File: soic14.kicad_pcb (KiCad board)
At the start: 2 copper layers, 11.2 x 27.4 mm, 2 parts, among them J1 Conn_02x07_Counter_Clockwise, J2 Conn_02x07_Counter_Clockwise

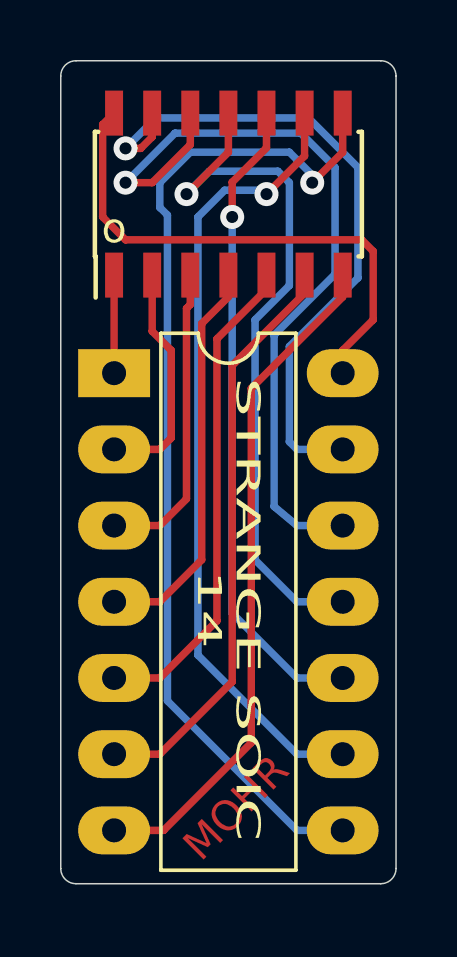
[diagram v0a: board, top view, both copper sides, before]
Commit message: fixed DRC warning.
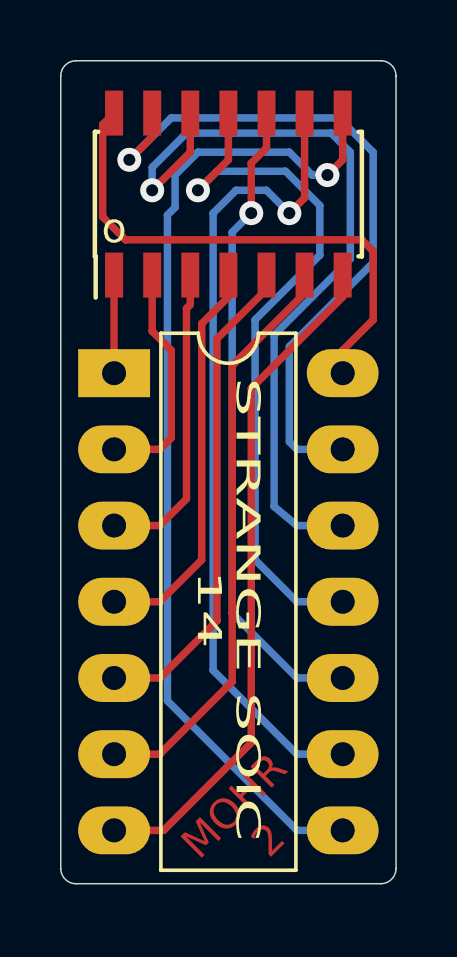
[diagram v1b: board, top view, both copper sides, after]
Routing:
- net Net-(J1-Pad13): track 22.7 -> 23.7 mm
- net Net-(J1-Pad9): track 26.7 -> 27.4 mm
- net Net-(J1-Pad8): track 33.8 -> 33.2 mm
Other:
- board text added: "MOHR 2"
- board text removed: "MOHR"

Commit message: version 3 adds capacitor and combs traces
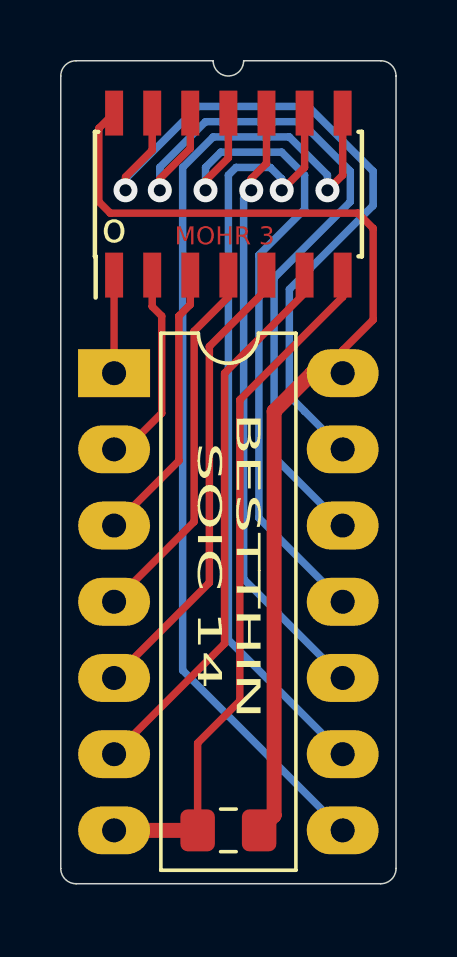
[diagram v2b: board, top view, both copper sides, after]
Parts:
- added C1: C, Capacitor_SMD:C_0805_2012Metric_Pad1.15x1.40mm_HandSolder, F.Cu at (149.9, 105.9)
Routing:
- net Net-(C1-Pad2): track 17.6 -> 34.9 mm
- net Net-(J1-Pad12): track 26.6 -> 25.2 mm
- net Net-(C1-Pad1): track 22.6 -> 23.9 mm
- net Net-(J1-Pad9): track 27.4 -> 26.2 mm
- net Net-(J1-Pad10): track 21.7 -> 20.5 mm
- net Net-(J1-Pad2): track 7.75 -> 6.82 mm
- net Net-(J1-Pad5): track 16.4 -> 15.5 mm
- net Net-(J1-Pad6): track 19.5 -> 18.6 mm
- net Net-(J1-Pad4): track 13.4 -> 12.5 mm
- net Net-(J1-Pad3): track 10.3 -> 9.40 mm
- net Net-(J1-Pad13): track 23.7 -> 24.6 mm
- net Net-(J1-Pad11): track 24.0 -> 23.5 mm
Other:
- outline, holes or cut-outs redrawn
- board text added: "BESTTHIN SOIC 14"
- board text added: "Everyone of you could play this game."
- board text added: "MOHR 3"
- board text removed: "MOHR 2"
- board text removed: "No one remembers your name."
- board text removed: "STRANGE SOIC 14"
